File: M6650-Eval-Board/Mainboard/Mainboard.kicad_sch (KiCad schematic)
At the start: 65 parts, among them J101 MB, J101 SB, J102 MR, J102 Parallel, J102 SR, J102 Serial, J103 MT, J103 ST, J104 ML, J104 SL, J12 5V, J13 5V, J14 Misc, J15 Line Out, J16 AUD, J9 Buttons, Q307 MMBT3904, SW1 P01, SW2 P02, SW3 P04, SW4 P08, SW5 RESET, U1 27C160

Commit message: Update eval board schematic consistency
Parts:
- renumbered J101 to J1, J102 to J10, J102 to J11, J102 to J2, J103 to J3, J104 to J4, J101 to J5, J102 to J6, J103 to J7, J104 to J8
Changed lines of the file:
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@@
   (symbol (lib_id "Connector_Generic:Conn_01x12") (at 140.97 38.1 180) (unit 1)
     (in_bom yes) (on_board yes) (dnp no) (fields_autoplaced)
-    (property "Reference" "J102" (at 138.43 36.195 0)
+    (property "Reference" "J6" (at 138.43 36.195 0)
       (effects (font (size 1.27 1.27)) (justify left))
     )
@@
   (symbol (lib_id "Connector_Generic:Conn_01x16") (at 116.84 52.07 90) (unit 1)
     (in_bom yes) (on_board yes) (dnp no) (fields_autoplaced)
-    (property "Reference" "J101" (at 118.11 46.99 90)
+    (property "Reference" "J5" (at 118.11 46.99 90)
       (effects (font (size 1.27 1.27)))
     )
@@
   (symbol (lib_id "Connector_Generic:Conn_01x16") (at 46.99 21.59 270) (unit 1)
     (in_bom yes) (on_board yes) (dnp no) (fields_autoplaced)
-    (property "Reference" "J103" (at 45.72 25.4 90)
+    (property "Reference" "J3" (at 45.72 25.4 90)
       (effects (font (size 1.27 1.27)))
     )
@@
   (symbol (lib_id "Connector_Generic:Conn_01x16") (at 44.45 52.07 90) (unit 1)
     (in_bom yes) (on_board yes) (dnp no) (fields_autoplaced)
-    (property "Reference" "J101" (at 45.72 46.99 90)
+    (property "Reference" "J1" (at 45.72 46.99 90)
       (effects (font (size 1.27 1.27)))
     )
@@
   (symbol (lib_id "Connector_Generic:Conn_01x16") (at 119.38 21.59 270) (unit 1)
     (in_bom yes) (on_board yes) (dnp no) (fields_autoplaced)
-    (property "Reference" "J103" (at 118.11 25.4 90)
+    (property "Reference" "J7" (at 118.11 25.4 90)
       (effects (font (size 1.27 1.27)))
     )
@@
   (symbol (lib_id "Connector_Generic:Conn_01x15") (at 48.26 104.14 0) (unit 1)
     (in_bom yes) (on_board yes) (dnp no) (fields_autoplaced)
-    (property "Reference" "J102" (at 50.8 103.505 0)
+    (property "Reference" "J10" (at 50.8 103.505 0)
       (effects (font (size 1.27 1.27)) (justify left))
     )
@@
   (symbol (lib_id "Connector_Generic:Conn_01x12") (at 22.86 35.56 0) (unit 1)
     (in_bom yes) (on_board yes) (dnp no) (fields_autoplaced)
-    (property "Reference" "J104" (at 25.4 36.195 0)
+    (property "Reference" "J4" (at 25.4 36.195 0)
       (effects (font (size 1.27 1.27)) (justify left))
     )
@@
   (symbol (lib_id "Connector_Generic:Conn_01x09") (at 27.94 111.76 0) (unit 1)
     (in_bom yes) (on_board yes) (dnp no) (fields_autoplaced)
-    (property "Reference" "J102" (at 30.48 111.125 0)
+    (property "Reference" "J11" (at 30.48 111.125 0)
       (effects (font (size 1.27 1.27)) (justify left))
     )
@@
   (symbol (lib_id "Connector_Generic:Conn_01x12") (at 95.25 35.56 0) (unit 1)
     (in_bom yes) (on_board yes) (dnp no) (fields_autoplaced)
-    (property "Reference" "J104" (at 97.79 36.195 0)
+    (property "Reference" "J8" (at 97.79 36.195 0)
       (effects (font (size 1.27 1.27)) (justify left))
     )
@@
   (symbol (lib_id "Connector_Generic:Conn_01x12") (at 68.58 38.1 180) (unit 1)
     (in_bom yes) (on_board yes) (dnp no)
-    (property "Reference" "J102" (at 66.04 36.195 0)
-      (effects (font (size 1.27 1.27)) (justify left))
-    )
+    (property "Reference" "J2" (at 66.04 36.195 0)
+      (effects (font (size 1.27 1.27)) (justify left))
+    )

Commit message: Fix XTCR pin for standalone mode
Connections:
- net 5V: now also J5.11 (Pin_11)
- net GND: no longer J5.11 (Pin_11)
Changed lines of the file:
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@@
     (effects (font (size 1.27 1.27)) (justify left bottom))
-  )
-  (label "GND" (at 124.46 57.15 270) (fields_autoplaced)
-    (effects (font (size 1.27 1.27)) (justify right bottom))
   )
   (label "I6SD" (at 22.86 109.22 180) (fields_autoplaced)
@@
     (effects (font (size 1.27 1.27)) (justify right bottom))
   )
+  (label "5V" (at 124.46 57.15 270) (fields_autoplaced)
+    (effects (font (size 1.27 1.27)) (justify right bottom))
+  )

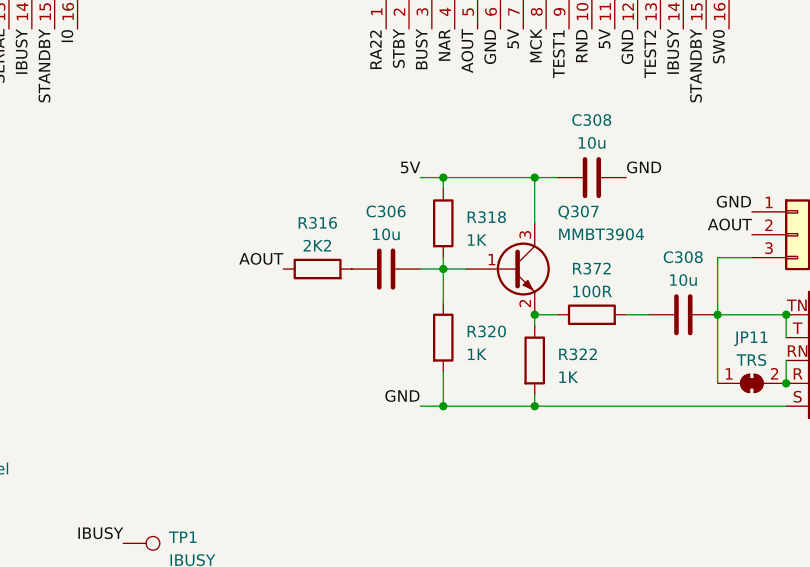
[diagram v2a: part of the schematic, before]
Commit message: Improve line-out amplifier for high-impedance DAC output
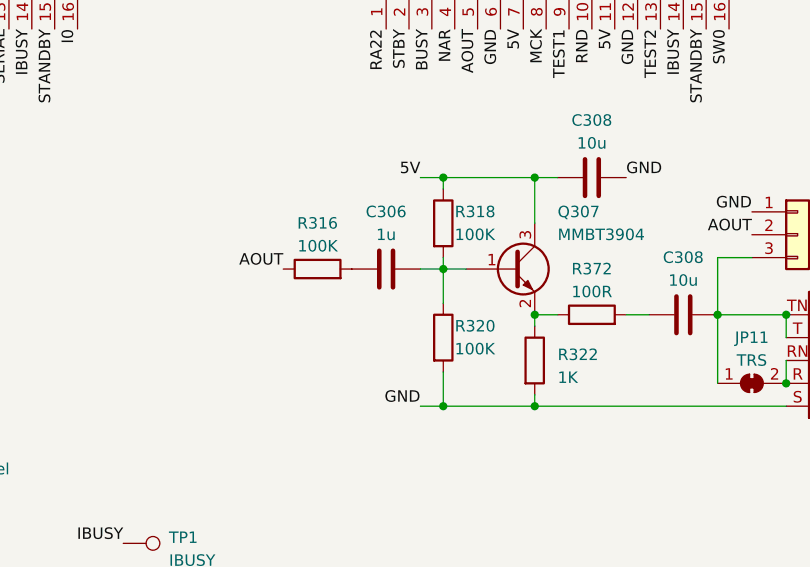
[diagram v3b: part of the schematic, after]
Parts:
- C306: value 10u -> 1u
- R316: value 2K2 -> 100K
- R318, R320: value 1K -> 100K
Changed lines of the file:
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@@
       (effects (font (size 1.27 1.27)))
     )
-    (property "Value" "2K2" (at 91.44 81.28 90)
+    (property "Value" "100K" (at 91.44 81.28 90)
       (effects (font (size 1.27 1.27)))
     )
@@
   )
   (symbol (lib_id "Device:R") (at 105.41 78.74 0) (unit 1)
-    (in_bom yes) (on_board yes) (dnp no) (fields_autoplaced)
-    (property "Reference" "R318" (at 107.95 78.105 0)
-      (effects (font (size 1.27 1.27)) (justify left))
-    )
-    (property "Value" "1K" (at 107.95 80.645 0)
+    (in_bom yes) (on_board yes) (dnp no)
+    (property "Reference" "R318" (at 106.68 77.47 0)
+      (effects (font (size 1.27 1.27)) (justify left))
+    )
+    (property "Value" "100K" (at 106.68 80.01 0)
       (effects (font (size 1.27 1.27)) (justify left))
     )
@@
   )
   (symbol (lib_id "Device:R") (at 105.41 91.44 0) (unit 1)
-    (in_bom yes) (on_board yes) (dnp no) (fields_autoplaced)
-    (property "Reference" "R320" (at 107.95 90.805 0)
-      (effects (font (size 1.27 1.27)) (justify left))
-    )
-    (property "Value" "1K" (at 107.95 93.345 0)
+    (in_bom yes) (on_board yes) (dnp no)
+    (property "Reference" "R320" (at 106.68 90.17 0)
+      (effects (font (size 1.27 1.27)) (justify left))
+    )
+    (property "Value" "100K" (at 106.68 92.71 0)
       (effects (font (size 1.27 1.27)) (justify left))
     )
@@
       (effects (font (size 1.27 1.27)))
     )
-    (property "Value" "10u" (at 99.06 80.01 90)
-      (effects (font (size 1.27 1.27)))
-    )
+    (property "Value" "1u" (at 99.06 80.01 90)
+      (effects (font (size 1.27 1.27)))
+    )

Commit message: Add debounce to manual parallel board, redo board edges and clearance rules
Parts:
- J10: footprint Connector_PinHeader_2.54mm:PinHeader_1x15_P2.54mm_Vertical -> Connector_PinSocket_2.54mm:PinSocket_1x15_P2.54mm_Vertical
- J11: footprint Connector_PinHeader_2.54mm:PinHeader_1x09_P2.54mm_Vertical -> Connector_PinSocket_2.54mm:PinSocket_1x09_P2.54mm_Vertical
- J16: footprint Connector_PinHeader_2.54mm:PinHeader_1x03_P2.54mm_Vertical -> Connector_PinSocket_2.54mm:PinSocket_1x03_P2.54mm_Vertical
- J9: footprint Connector_PinHeader_2.54mm:PinHeader_1x06_P2.54mm_Vertical -> Connector_PinSocket_2.54mm:PinSocket_1x06_P2.54mm_Vertical
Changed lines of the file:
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@@
       (effects (font (size 1.27 1.27)) (justify left))
     )
-    (property "Footprint" "Connector_PinHeader_2.54mm:PinHeader_1x03_P2.54mm_Vertical" (at 144.78 80.01 0)
+    (property "Footprint" "Connector_PinSocket_2.54mm:PinSocket_1x03_P2.54mm_Vertical" (at 144.78 80.01 0)
       (effects (font (size 1.27 1.27)) hide)
     )
@@
       (effects (font (size 1.27 1.27)) (justify left))
     )
-    (property "Footprint" "Connector_PinHeader_2.54mm:PinHeader_1x15_P2.54mm_Vertical" (at 48.26 104.14 0)
+    (property "Footprint" "Connector_PinSocket_2.54mm:PinSocket_1x15_P2.54mm_Vertical" (at 48.26 104.14 0)
       (effects (font (size 1.27 1.27)) hide)
     )
@@
       (effects (font (size 1.27 1.27)) (justify left))
     )
-    (property "Footprint" "Connector_PinHeader_2.54mm:PinHeader_1x09_P2.54mm_Vertical" (at 27.94 111.76 0)
+    (property "Footprint" "Connector_PinSocket_2.54mm:PinSocket_1x09_P2.54mm_Vertical" (at 27.94 111.76 0)
       (effects (font (size 1.27 1.27)) hide)
     )
@@
       (effects (font (size 1.27 1.27)) (justify left))
     )
-    (property "Footprint" "Connector_PinHeader_2.54mm:PinHeader_1x06_P2.54mm_Vertical" (at 55.88 186.69 0)
-      (effects (font (size 1.27 1.27)) hide)
-    )
+    (property "Footprint" "Connector_PinSocket_2.54mm:PinSocket_1x06_P2.54mm_Vertical" (at 55.88 186.69 0)
+      (effects (font (size 1.27 1.27)) hide)
+    )
